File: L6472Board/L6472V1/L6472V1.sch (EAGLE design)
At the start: 34 parts

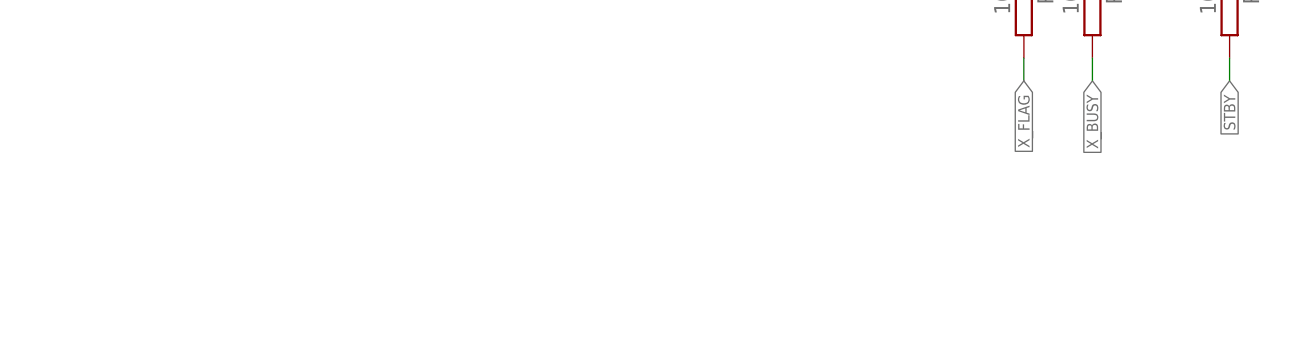
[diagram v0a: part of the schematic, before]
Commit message: Fixing schematics for design review, adding block diagram, upgrading version to prototype version 2
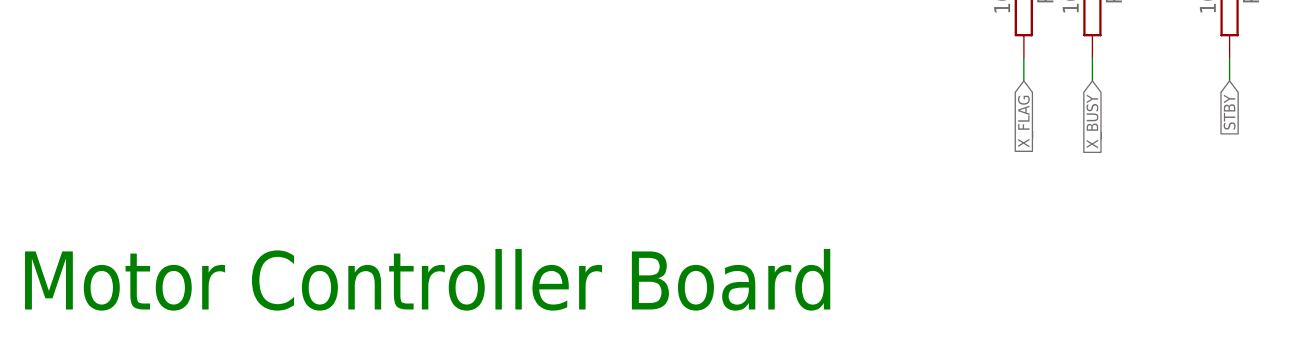
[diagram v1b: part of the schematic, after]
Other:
- note added: "Motor Controller Board"
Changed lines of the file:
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@@
 <sheet>
 <plain>
+<text x="-55.88" y="-119.38" size="6.4516" layer="91">Motor Controller Board</text>
 </plain>
 <instances>

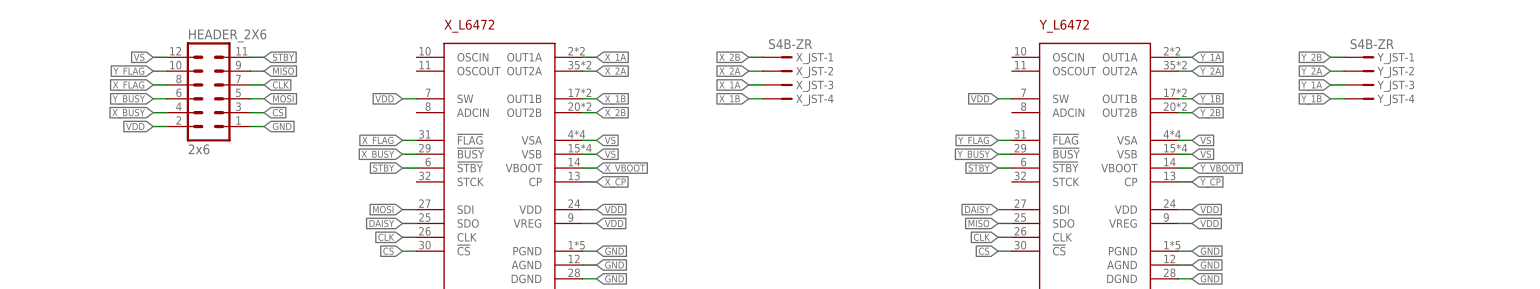
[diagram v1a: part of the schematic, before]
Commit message: Created New Footprints
Footprints:
JST
BAC
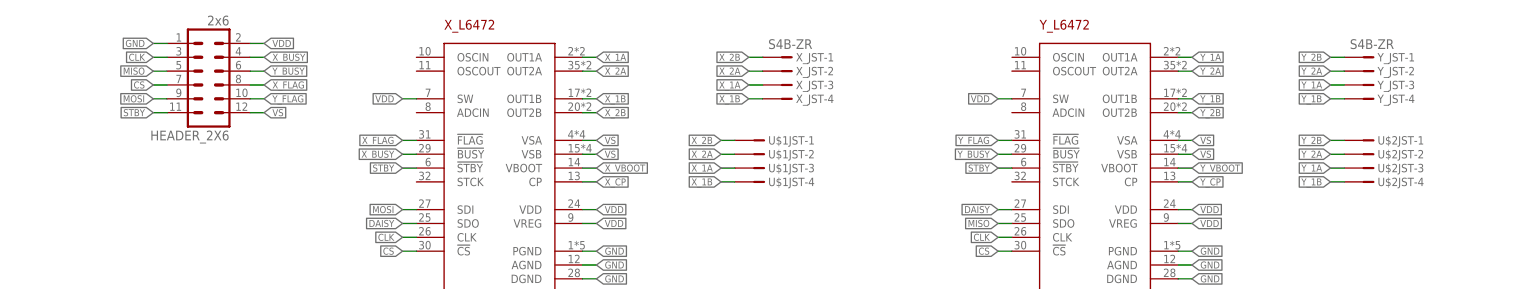
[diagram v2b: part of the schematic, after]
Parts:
- added U$1, U$2: JST, L6472LIB:JST
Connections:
- net CLK: now also HEADER_2X6.3; no longer HEADER_2X6.7
- net CS: now also HEADER_2X6.7; no longer HEADER_2X6.3
- net MISO: now also HEADER_2X6.5; no longer HEADER_2X6.9
- net MOSI: now also HEADER_2X6.9; no longer HEADER_2X6.5
- net X_1A: now also U$1JST-3.1
- net X_1B: now also U$1JST-4.1
- net X_2A: now also U$1JST-2.1
- net X_2B: now also U$1JST-1.1
- net Y_1A: now also U$2JST-3.1
- net Y_1B: now also U$2JST-4.1
- net Y_2A: now also U$2JST-2.1
- net Y_2B: now also U$2JST-1.1
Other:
- moved on the sheet: HEADER_2X6
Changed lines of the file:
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@@
 <part name="R4" library="resistor" deviceset="R-EU_" device="M1206" value="10k"/>
 <part name="R5" library="resistor" deviceset="R-EU_" device="M1206" value="10k"/>
+<part name="U$1" library="L6472LIB" deviceset="JST" device=""/>
+<part name="U$2" library="L6472LIB" deviceset="JST" device=""/>
 </parts>
 <sheets>
@@
 <instance part="Y_JST" gate="-3" x="210.82" y="63.5"/>
 <instance part="Y_JST" gate="-4" x="210.82" y="60.96"/>
-<instance part="HEADER_2X6" gate="1" x="-2.54" y="63.5"/>
+<instance part="HEADER_2X6" gate="1" x="-2.54" y="63.5" rot="R180"/>
 <instance part="X_C8" gate="G$1" x="104.14" y="0"/>
 <instance part="X_C9" gate="G$1" x="116.84" y="0"/>
@@
 <instance part="R4" gate="G$1" x="93.98" y="-86.36" rot="R270"/>
 <instance part="R5" gate="G$1" x="101.6" y="-86.36" rot="R270"/>
+<instance part="U$1" gate="JST-1" x="99.06" y="53.34"/>
+<instance part="U$1" gate="JST-2" x="99.06" y="50.8"/>
+<instance part="U$1" gate="JST-3" x="99.06" y="48.26"/>
+<instance part="U$1" gate="JST-4" x="99.06" y="45.72"/>
+<instance part="U$2" gate="JST-1" x="210.82" y="53.34"/>
+<instance part="U$2" gate="JST-2" x="210.82" y="50.8"/>
+<instance part="U$2" gate="JST-3" x="210.82" y="48.26"/>
+<instance part="U$2" gate="JST-4" x="210.82" y="45.72"/>
 </instances>
 <busses>
@@
 <segment>
 <pinref part="HEADER_2X6" gate="1" pin="2"/>
-<wire x1="-10.16" y1="55.88" x2="-12.7" y2="55.88" width="0.1524" layer="91"/>
-<label x="-12.7" y="55.88" size="1.27" layer="95" rot="R180" xref="yes"/>
+<wire x1="5.08" y1="71.12" x2="7.62" y2="71.12" width="0.1524" layer="91"/>
+<label x="7.62" y="71.12" size="1.27" layer="95" xref="yes"/>
 </segment>
 <segment>
@@
 <label x="96.52" y="63.5" size="1.27" layer="95" rot="R180" xref="yes"/>
 </segment>
+<segment>
+<pinref part="U$1" gate="JST-3" pin="1"/>
+<wire x1="93.98" y1="48.26" x2="91.44" y2="48.26" width="0.1524" layer="91"/>
+<label x="91.44" y="48.26" size="1.27" layer="95" rot="R180" xref="yes"/>
+</segment>
 </net>
 <net name="X_2A" class="0">
@@
 <label x="96.52" y="66.04" size="1.27" layer="95" rot="R180" xref="yes"/>
 </segment>
+<segment>
+<pinref part="U$1" gate="JST-2" pin="1"/>
+<wire x1="93.98" y1="50.8" x2="91.44" y2="50.8" width="0.1524" layer="91"/>
+<label x="91.44" y="50.8" size="1.27" layer="95" rot="R180" xref="yes"/>
+</segment>
 </net>
 <net name="X_1B" class="0">
@@
 <label x="96.52" y="60.96" size="1.27" layer="95" rot="R180" xref="yes"/>
 </segment>
+<segment>
+<pinref part="U$1" gate="JST-4" pin="1"/>
+<wire x1="93.98" y1="45.72" x2="91.44" y2="45.72" width="0.1524" layer="91"/>
+<label x="91.44" y="45.72" size="1.27" layer="95" rot="R180" xref="yes"/>
+</segment>
 </net>
 <net name="X_2B" class="0">
@@
 <wire x1="99.06" y1="68.58" x2="96.52" y2="68.58" width="0.1524" layer="91"/>
 <label x="96.52" y="68.58" size="1.27" layer="95" rot="R180" xref="yes"/>
+</segment>
+<segment>
+<pinref part="U$1" gate="JST-1" pin="1"/>
+<wire x1="93.98" y1="53.34" x2="91.44" y2="53.34" width="0.1524" layer="91"/>
+<label x="91.44" y="53.34" size="1.27" layer="95" rot="R180" xref="yes"/>
 </segment>
 </net>
@@
 <segment>
 <pinref part="HEADER_2X6" gate="1" pin="12"/>
-<wire x1="-10.16" y1="68.58" x2="-12.7" y2="68.58" width="0.1524" layer="91"/>
-<label x="-12.7" y="68.58" size="1.27" layer="95" rot="R180" xref="yes"/>
+<wire x1="5.08" y1="58.42" x2="7.62" y2="58.42" width="0.1524" layer="91"/>
+<label x="7.62" y="58.42" size="1.27" layer="95" xref="yes"/>
 </segment>
 </net>
@@
 <segment>
 <pinref part="HEADER_2X6" gate="1" pin="1"/>
-<wire x1="5.08" y1="55.88" x2="7.62" y2="55.88" width="0.1524" layer="91"/>
-<label x="7.62" y="55.88" size="1.27" layer="95" xref="yes"/>
+<wire x1="-10.16" y1="71.12" x2="-12.7" y2="71.12" width="0.1524" layer="91"/>
+<label x="-12.7" y="71.12" size="1.27" layer="95" rot="R180" xref="yes"/>
 </segment>
 <segment>
@@
 <segment>
 <pinref part="HEADER_2X6" gate="1" pin="8"/>
-<wire x1="-10.16" y1="63.5" x2="-12.7" y2="63.5" width="0.1524" layer="91"/>
-<label x="-12.7" y="63.5" size="1.27" layer="95" rot="R180" xref="yes"/>
+<wire x1="5.08" y1="63.5" x2="7.62" y2="63.5" width="0.1524" layer="91"/>
+<label x="7.62" y="63.5" size="1.27" layer="95" xref="yes"/>
 </segment>
 <segment>
@@
 <segment>
 <pinref part="HEADER_2X6" gate="1" pin="4"/>
-<wire x1="-10.16" y1="58.42" x2="-12.7" y2="58.42" width="0.1524" layer="91"/>
-<label x="-12.7" y="58.42" size="1.27" layer="95" rot="R180" xref="yes"/>
+<wire x1="5.08" y1="68.58" x2="7.62" y2="68.58" width="0.1524" layer="91"/>
+<label x="7.62" y="68.58" size="1.27" layer="95" xref="yes"/>
 </segment>
 <segment>
@@
 <segment>
 <pinref part="HEADER_2X6" gate="1" pin="11"/>
-<wire x1="5.08" y1="68.58" x2="7.62" y2="68.58" width="0.1524" layer="91"/>
-<label x="7.62" y="68.58" size="1.27" layer="95" xref="yes"/>
+<wire x1="-10.16" y1="58.42" x2="-12.7" y2="58.42" width="0.1524" layer="91"/>
+<label x="-12.7" y="58.42" size="1.27" layer="95" rot="R180" xref="yes"/>
 </segment>
 <segment>
@@
 </segment>
 <segment>
-<pinref part="HEADER_2X6" gate="1" pin="5"/>
-<wire x1="5.08" y1="60.96" x2="7.62" y2="60.96" width="0.1524" layer="91"/>
-<label x="7.62" y="60.96" size="1.27" layer="95" xref="yes"/>
+<pinref part="HEADER_2X6" gate="1" pin="9"/>
+<wire x1="-10.16" y1="60.96" x2="-12.7" y2="60.96" width="0.1524" layer="91"/>
+<label x="-12.7" y="60.96" size="1.27" layer="95" rot="R180" xref="yes"/>
 </segment>
 </net>
@@
 </segment>
 <segment>
-<pinref part="HEADER_2X6" gate="1" pin="7"/>
-<wire x1="5.08" y1="63.5" x2="7.62" y2="63.5" width="0.1524" layer="91"/>
-<label x="7.62" y="63.5" size="1.27" layer="95" xref="yes"/>
+<pinref part="HEADER_2X6" gate="1" pin="3"/>
+<wire x1="-10.16" y1="68.58" x2="-12.7" y2="68.58" width="0.1524" layer="91"/>
+<label x="-12.7" y="68.58" size="1.27" layer="95" rot="R180" xref="yes"/>
 </segment>
 </net>
@@
 </segment>
 <segment>
-<pinref part="HEADER_2X6" gate="1" pin="3"/>
-<wire x1="5.08" y1="58.42" x2="7.62" y2="58.42" width="0.1524" layer="91"/>
-<label x="7.62" y="58.42" size="1.27" layer="95" xref="yes"/>
+<pinref part="HEADER_2X6" gate="1" pin="7"/>
+<wire x1="-10.16" y1="63.5" x2="-12.7" y2="63.5" width="0.1524" layer="91"/>
+<label x="-12.7" y="63.5" size="1.27" layer="95" rot="R180" xref="yes"/>
 </segment>
 </net>
@@
 <segment>
 <pinref part="HEADER_2X6" gate="1" pin="10"/>
-<wire x1="-10.16" y1="66.04" x2="-12.7" y2="66.04" width="0.1524" layer="91"/>
-<label x="-12.7" y="66.04" size="1.27" layer="95" rot="R180" xref="yes"/>
+<wire x1="5.08" y1="60.96" x2="7.62" y2="60.96" width="0.1524" layer="91"/>
+<label x="7.62" y="60.96" size="1.27" layer="95" xref="yes"/>
 </segment>
 <segment>
@@
 <segment>
 <pinref part="HEADER_2X6" gate="1" pin="6"/>
-<wire x1="-10.16" y1="60.96" x2="-12.7" y2="60.96" width="0.1524" layer="91"/>
-<label x="-12.7" y="60.96" size="1.27" layer="95" rot="R180" xref="yes"/>
+<wire x1="5.08" y1="66.04" x2="7.62" y2="66.04" width="0.1524" layer="91"/>
+<label x="7.62" y="66.04" size="1.27" layer="95" xref="yes"/>
 </segment>
 <segment>
@@
 </segment>
 <segment>
-<pinref part="HEADER_2X6" gate="1" pin="9"/>
-<wire x1="5.08" y1="66.04" x2="7.62" y2="66.04" width="0.1524" layer="91"/>
-<label x="7.62" y="66.04" size="1.27" layer="95" xref="yes"/>
+<pinref part="HEADER_2X6" gate="1" pin="5"/>
+<wire x1="-10.16" y1="66.04" x2="-12.7" y2="66.04" width="0.1524" layer="91"/>
+<label x="-12.7" y="66.04" size="1.27" layer="95" rot="R180" xref="yes"/>
 </segment>
 </net>
@@
 <label x="203.2" y="63.5" size="1.27" layer="95" rot="R180" xref="yes"/>
 </segment>
+<segment>
+<pinref part="U$2" gate="JST-3" pin="1"/>
+<wire x1="205.74" y1="48.26" x2="203.2" y2="48.26" width="0.1524" layer="91"/>
+<label x="203.2" y="48.26" size="1.27" layer="95" rot="R180" xref="yes"/>
+</segment>
 </net>
 <net name="Y_2A" class="0">
@@
 <label x="203.2" y="66.04" size="1.27" layer="95" rot="R180" xref="yes"/>
 </segment>
+<segment>
+<pinref part="U$2" gate="JST-2" pin="1"/>
+<wire x1="205.74" y1="50.8" x2="203.2" y2="50.8" width="0.1524" layer="91"/>
+<label x="203.2" y="50.8" size="1.27" layer="95" rot="R180" xref="yes"/>
+</segment>
 </net>
 <net name="Y_1B" class="0">
@@
 <label x="203.2" y="60.96" size="1.27" layer="95" rot="R180" xref="yes"/>
 </segment>
+<segment>
+<pinref part="U$2" gate="JST-4" pin="1"/>
+<wire x1="205.74" y1="45.72" x2="203.2" y2="45.72" width="0.1524" layer="91"/>
+<label x="203.2" y="45.72" size="1.27" layer="95" rot="R180" xref="yes"/>
+</segment>
 </net>
 <net name="Y_2B" class="0">
@@
 <label x="203.2" y="68.58" size="1.27" layer="95" rot="R180" xref="yes"/>
 </segment>
-</net>
+<segment>
+<pinref part="U$2" gate="JST-1" pin="1"/>
+<wire x1="205.74" y1="53.34" x2="203.2" y2="53.34" width="0.1524" layer="91"/>
+<label x="203.2" y="53.34" size="1.27" layer="95" rot="R180" xref="yes"/>
+</segment>
+</net>

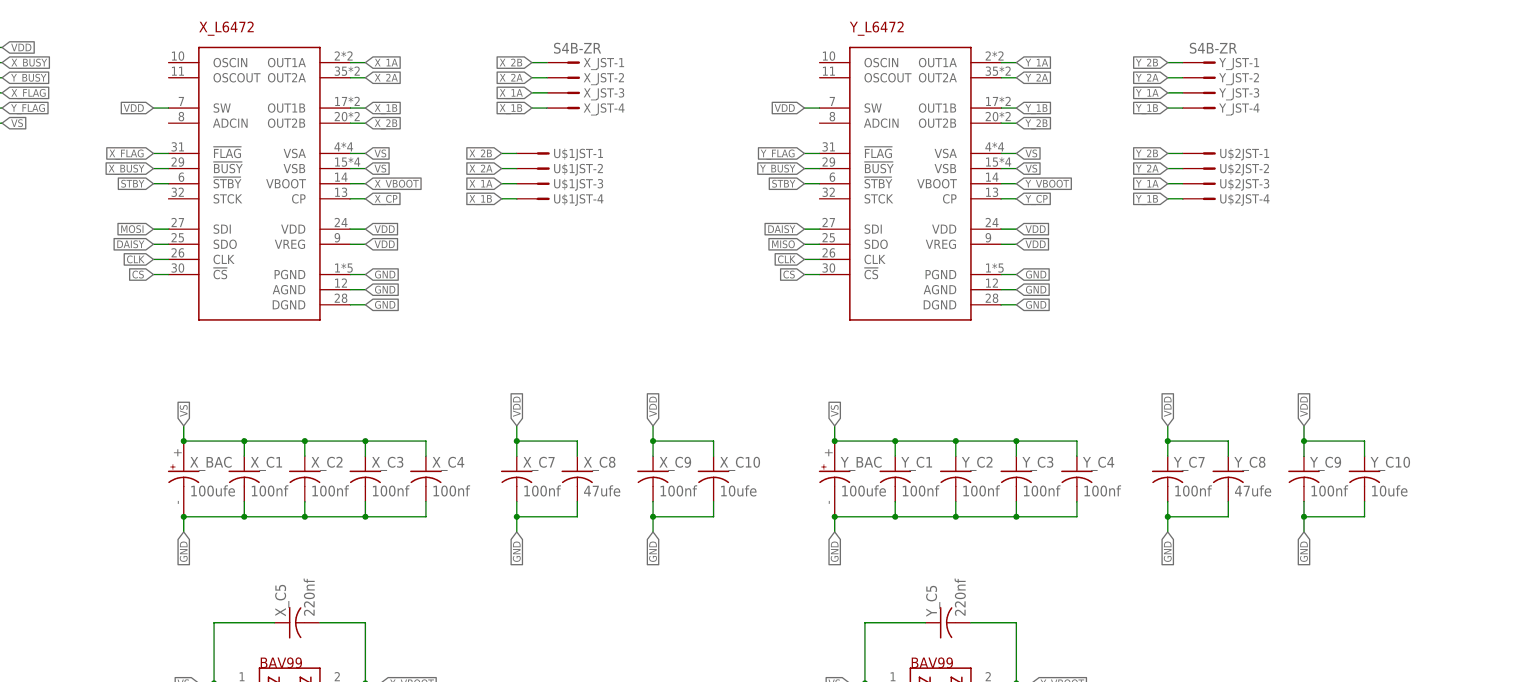
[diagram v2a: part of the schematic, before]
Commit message: Revision of Motorcontroller Board
Footprints for the stepper motor connectors and BACs were replaced.
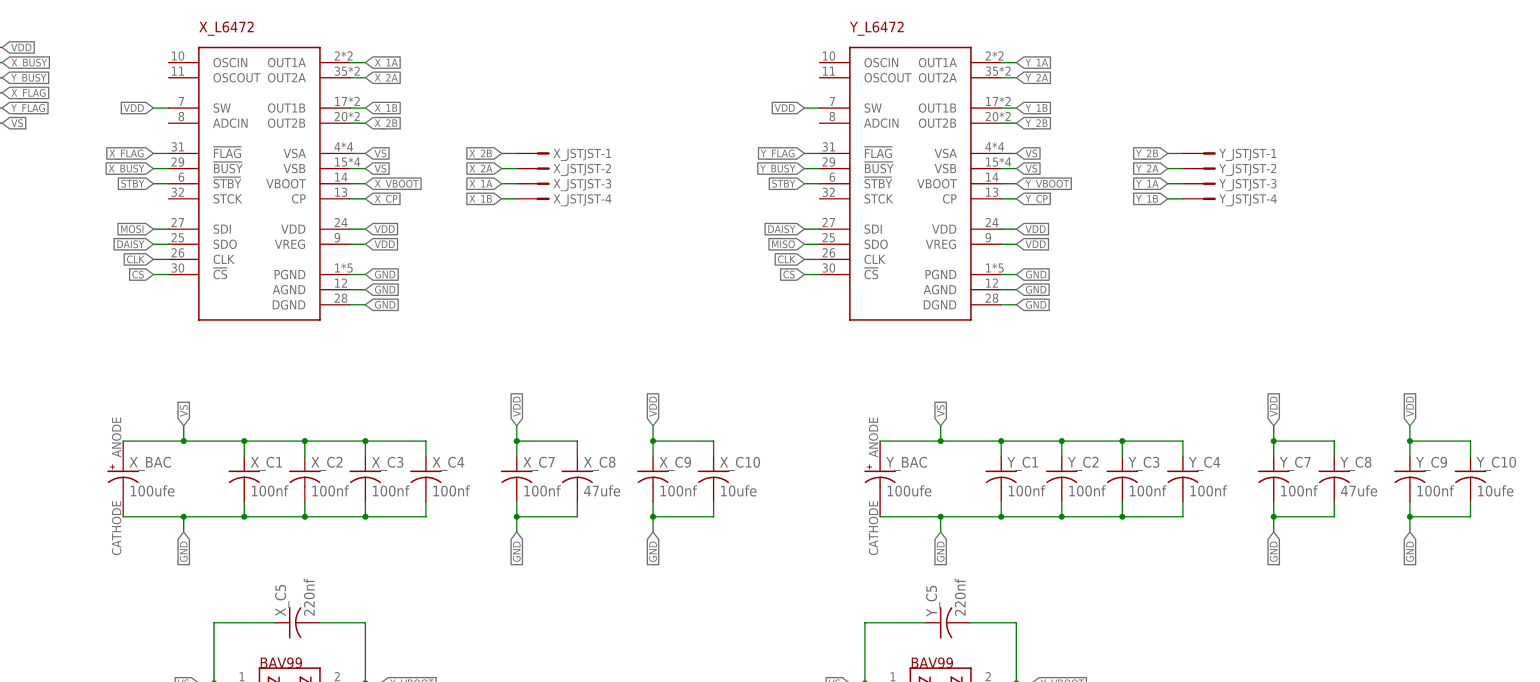
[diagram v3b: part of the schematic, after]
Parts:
- removed U$1, U$2: JST, L6472LIB:JST
- X_BAC, Y_BAC: device L6472LIB:EEE-FC1C471AP -> L6472LIB:EEE-1AA101WR
- X_JST, Y_JST: value S4B-ZR -> JST; device con-jst:S4B-ZR -> L6472LIB:JST
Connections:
- net X_1A: now also X_JSTJST-3.1; no longer U$1JST-3.1, X_JST-3.1
- net X_1B: now also X_JSTJST-4.1; no longer U$1JST-4.1, X_JST-4.1
- net X_2A: now also X_JSTJST-2.1; no longer U$1JST-2.1, X_JST-2.1
- net X_2B: now also X_JSTJST-1.1; no longer U$1JST-1.1, X_JST-1.1
- net Y_1A: now also Y_JSTJST-3.1; no longer U$2JST-3.1, Y_JST-3.1
- net Y_1B: now also Y_JSTJST-4.1; no longer U$2JST-4.1, Y_JST-4.1
- net Y_2A: now also Y_JSTJST-2.1; no longer U$2JST-2.1, Y_JST-2.1
- net Y_2B: now also Y_JSTJST-1.1; no longer U$2JST-1.1, Y_JST-1.1
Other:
- moved on the sheet: X_BAC, Y_BAC, Y_C1, Y_C10, Y_C2, Y_C3, Y_C4, Y_C7, Y_C8, Y_C9
